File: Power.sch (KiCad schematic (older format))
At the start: 30 parts, among them J4 USB4125-GF-A, J5 S2B-PH-SM4-TB, U10 MCP73831T-2ATI_OT, U11 MIC2288YD5, U8 RT6150AGQW, U9 LP5907MFX-3.2

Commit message: Resolve DRC errors and add proper flagging
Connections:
- wire segments 83 -> 87
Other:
- moved on the sheet: C20, C23, J5, R21, R22, R25, U10

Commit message: layout wip
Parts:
- renumbered C17 to C18, C18 to C19, C19 to C20, C20 to C21, C21 to C22, C22 to C23, C23 to C24, C24 to C25, C25 to C26, J4 to J3, J5 to J4, R16 to R18, R17 to R19, R18 to R20, R19 to R21, R20 to R22, R21 to R23, R22 to R24, R23 to R25, R24 to R26, R25 to R27, R26 to R28, R27 to R29, U9 to U10, U10 to U11, U11 to U12, U8 to U9

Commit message: Add resistor details
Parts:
- R19, R20: Description (none) -> RES 5.1K OHM 1% 1/16W 0402; Manufacturer (none) -> Stackpole Electronics Inc; Part Number (none) -> RMCF0402FT5K10; Temp Range (none) -> -55°C +155°C
- R21: Description (none) -> RES 487K OHM 1% 1/16W 0402; Manufacturer (none) -> Stackpole Electronics Inc; Part Number (none) -> RMCF0402FT487K; Temp Range (none) -> -55°C +155°C
- R22: Description (none) -> RES 86.6K OHM 1% 1/16W 0402; Manufacturer (none) -> Stackpole Electronics Inc; Part Number (none) -> RMCF0402FT86K6; Temp Range (none) -> -55°C +155°C
- R23: Description (none) -> RES 300K OHM 1% 1/16W 0402; Manufacturer (none) -> Stackpole Electronics Inc; Part Number (none) -> RMCF0402FT300K; Temp Range (none) -> -55°C +155°C
- R24: Description (none) -> RES 180K OHM 1% 1/16W 0402; Manufacturer (none) -> Stackpole Electronics Inc; Part Number (none) -> RMCF0402FT180K; Temp Range (none) -> -55°C +155°C
- R25: Description (none) -> RES 0 OHM JUMPER 1/16W 0402; Manufacturer (none) -> Stackpole Electronics Inc; Part Number (none) -> RMCF0402ZT0R00; Temp Range (none) -> -55°C +155°C
- R27: Description (none) -> RES 10K OHM 1% 1/16W 0402; Manufacturer (none) -> Stackpole Electronics Inc; Part Number (none) -> RMCF0402FT10K0; Temp Range (none) -> -55°C +155°C
- R28: Description (none) -> RES 9.1K OHM 1% 1/16W 0402; Manufacturer (none) -> Stackpole Electronics Inc; Part Number (none) -> RMCF0402FT9K10; Temp Range (none) -> -55°C +155°C
- R29: Description (none) -> RES 3K OHM 1% 1/16W 0402; Manufacturer (none) -> Stackpole Electronics Inc; Part Number (none) -> RMCF0402FT3K00; Temp Range (none) -> -55°C +155°C
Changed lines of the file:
@@
 F 1 "86.6k" H 4720 4455 50  0000 L CNN
 F 2 "JetkovKiCADLib:R_0402_NoSilk" V 4580 4500 50  0001 C CNN
-F 3 "~" H 4650 4500 50  0001 C CNN
+F 3 "https://www.seielect.com/catalog/sei-rmcf_rmcp.pdf" H 4650 4500 50  0001 C CNN
+F 4 "RES 86.6K OHM 1% 1/16W 0402" H 4650 4500 50  0001 C CNN "Description"
+F 5 "Stackpole Electronics Inc" H 4650 4500 50  0001 C CNN "Manufacturer"
+F 6 "RMCF0402FT86K6" H 4650 4500 50  0001 C CNN "Part Number"
+F 7 "-55°C +155°C" H 4650 4500 50  0001 C CNN "Temp Range"
 	1    4650 4500
 	1    0    0    -1
@@
 F 1 "10k" H 6670 1905 50  0000 L CNN
 F 2 "JetkovKiCADLib:R_0402_NoSilk" V 6530 1950 50  0001 C CNN
-F 3 "~" H 6600 1950 50  0001 C CNN
+F 3 "https://www.seielect.com/catalog/sei-rmcf_rmcp.pdf" H 6600 1950 50  0001 C CNN
+F 4 "RES 10K OHM 1% 1/16W 0402" H 6600 1950 50  0001 C CNN "Description"
+F 5 "Stackpole Electronics Inc" H 6600 1950 50  0001 C CNN "Manufacturer"
+F 6 "RMCF0402FT10K0" H 6600 1950 50  0001 C CNN "Part Number"
+F 7 "-55°C +155°C" H 6600 1950 50  0001 C CNN "Temp Range"
 	1    6600 1950
 	1    0    0    -1
@@
 F 1 "487k" H 4720 4055 50  0000 L CNN
 F 2 "JetkovKiCADLib:R_0402_NoSilk" V 4580 4100 50  0001 C CNN
-F 3 "~" H 4650 4100 50  0001 C CNN
+F 3 "https://www.seielect.com/catalog/sei-rmcf_rmcp.pdf" H 4650 4100 50  0001 C CNN
+F 4 "RES 487K OHM 1% 1/16W 0402" H 4650 4100 50  0001 C CNN "Description"
+F 5 "Stackpole Electronics Inc" H 4650 4100 50  0001 C CNN "Manufacturer"
+F 6 "RMCF0402FT487K" H 4650 4100 50  0001 C CNN "Part Number"
+F 7 "-55°C +155°C" H 4650 4100 50  0001 C CNN "Temp Range"
 	1    4650 4100
 	1    0    0    -1
@@
 F 1 "9.1k" H 7720 3655 50  0000 L CNN
 F 2 "JetkovKiCADLib:R_0402_NoSilk" V 7580 3700 50  0001 C CNN
-F 3 "~" H 7650 3700 50  0001 C CNN
+F 3 "https://www.seielect.com/catalog/sei-rmcf_rmcp.pdf" H 7650 3700 50  0001 C CNN
+F 4 "RES 9.1K OHM 1% 1/16W 0402" H 7650 3700 50  0001 C CNN "Description"
+F 5 "Stackpole Electronics Inc" H 7650 3700 50  0001 C CNN "Manufacturer"
+F 6 "RMCF0402FT9K10" H 7650 3700 50  0001 C CNN "Part Number"
+F 7 "-55°C +155°C" H 7650 3700 50  0001 C CNN "Temp Range"
 	1    7650 3700
 	1    0    0    -1
@@
 F 1 "3k" H 7720 4055 50  0000 L CNN
 F 2 "JetkovKiCADLib:R_0402_NoSilk" V 7580 4100 50  0001 C CNN
-F 3 "~" H 7650 4100 50  0001 C CNN
+F 3 "https://www.seielect.com/catalog/sei-rmcf_rmcp.pdf" H 7650 4100 50  0001 C CNN
+F 4 "RES 3K OHM 1% 1/16W 0402" H 7650 4100 50  0001 C CNN "Description"
+F 5 "Stackpole Electronics Inc" H 7650 4100 50  0001 C CNN "Manufacturer"
+F 6 "RMCF0402FT3K00" H 7650 4100 50  0001 C CNN "Part Number"
+F 7 "-55°C +155°C" H 7650 4100 50  0001 C CNN "Temp Range"
 	1    7650 4100
 	1    0    0    -1
@@
 F 1 "5.1k" H 4070 1955 50  0000 L CNN
 F 2 "JetkovKiCADLib:R_0402_NoSilk" V 3930 2000 50  0001 C CNN
-F 3 "~" H 4000 2000 50  0001 C CNN
+F 3 "https://www.seielect.com/catalog/sei-rmcf_rmcp.pdf" H 4000 2000 50  0001 C CNN
+F 4 "RES 5.1K OHM 1% 1/16W 0402" H 4000 2000 50  0001 C CNN "Description"
+F 5 "Stackpole Electronics Inc" H 4000 2000 50  0001 C CNN "Manufacturer"
+F 6 "RMCF0402FT5K10" H 4000 2000 50  0001 C CNN "Part Number"
+F 7 "-55°C +155°C" H 4000 2000 50  0001 C CNN "Temp Range"
 	1    4000 2000
 	-1   0    0    -1
@@
 F 1 "5.1k" H 4270 1955 50  0000 L CNN
 F 2 "JetkovKiCADLib:R_0402_NoSilk" V 4130 2000 50  0001 C CNN
-F 3 "~" H 4200 2000 50  0001 C CNN
+F 3 "https://www.seielect.com/catalog/sei-rmcf_rmcp.pdf" H 4200 2000 50  0001 C CNN
+F 4 "RES 5.1K OHM 1% 1/16W 0402" H 4200 2000 50  0001 C CNN "Description"
+F 5 "Stackpole Electronics Inc" H 4200 2000 50  0001 C CNN "Manufacturer"
+F 6 "RMCF0402FT5K10" H 4200 2000 50  0001 C CNN "Part Number"
+F 7 "-55°C +155°C" H 4200 2000 50  0001 C CNN "Temp Range"
 	1    4200 2000
 	1    0    0    -1
@@
 F 1 "0R" V 5450 5150 50  0000 L CNN
 F 2 "JetkovKiCADLib:R_0402_NoSilk" V 5480 5300 50  0001 C CNN
-F 3 "~" H 5550 5300 50  0001 C CNN
+F 3 "https://www.seielect.com/catalog/sei-rmcf_rmcp.pdf" H 5550 5300 50  0001 C CNN
+F 4 "RES 0 OHM JUMPER 1/16W 0402" H 5550 5300 50  0001 C CNN "Description"
+F 5 "Stackpole Electronics Inc" H 5550 5300 50  0001 C CNN "Manufacturer"
+F 6 "RMCF0402ZT0R00" H 5550 5300 50  0001 C CNN "Part Number"
+F 7 "-55°C +155°C" H 5550 5300 50  0001 C CNN "Temp Range"
 	1    5550 5300
 	0    1    1    0
@@
 F 1 "180k" V 5550 2000 50  0000 L CNN
 F 2 "JetkovKiCADLib:R_0402_NoSilk" V 5380 2100 50  0001 C CNN
-F 3 "~" H 5450 2100 50  0001 C CNN
+F 3 "https://www.seielect.com/catalog/sei-rmcf_rmcp.pdf" H 5450 2100 50  0001 C CNN
+F 4 "RES 180K OHM 1% 1/16W 0402" H 5450 2100 50  0001 C CNN "Description"
+F 5 "Stackpole Electronics Inc" H 5450 2100 50  0001 C CNN "Manufacturer"
+F 6 "RMCF0402FT180K" H 5450 2100 50  0001 C CNN "Part Number"
+F 7 "-55°C +155°C" H 5450 2100 50  0001 C CNN "Temp Range"
 	1    5450 2100
 	0    -1   -1   0
@@
 F 1 "300k" H 5320 2255 50  0000 L CNN
 F 2 "JetkovKiCADLib:R_0402_NoSilk" V 5180 2300 50  0001 C CNN
-F 3 "~" H 5250 2300 50  0001 C CNN
+F 3 "https://www.seielect.com/catalog/sei-rmcf_rmcp.pdf" H 5250 2300 50  0001 C CNN
+F 4 "RES 300K OHM 1% 1/16W 0402" H 5250 2300 50  0001 C CNN "Description"
+F 5 "Stackpole Electronics Inc" H 5250 2300 50  0001 C CNN "Manufacturer"
+F 6 "RMCF0402FT300K" H 5250 2300 50  0001 C CNN "Part Number"
+F 7 "-55°C +155°C" H 5250 2300 50  0001 C CNN "Temp Range"
 	1    5250 2300
 	1    0    0    -1

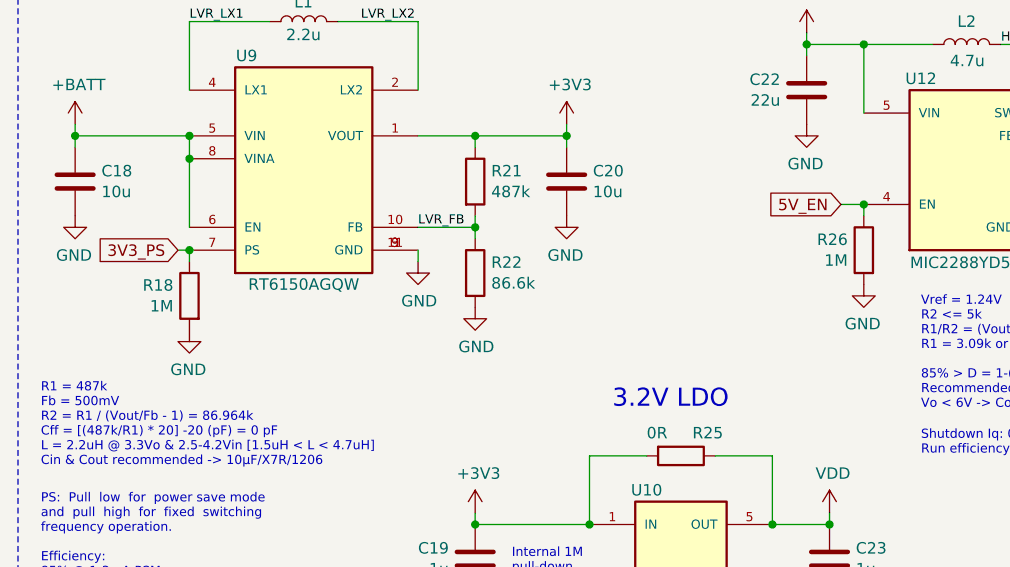
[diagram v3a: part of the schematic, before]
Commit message: Fill in component info, reduce uniqe resistors. cleanup
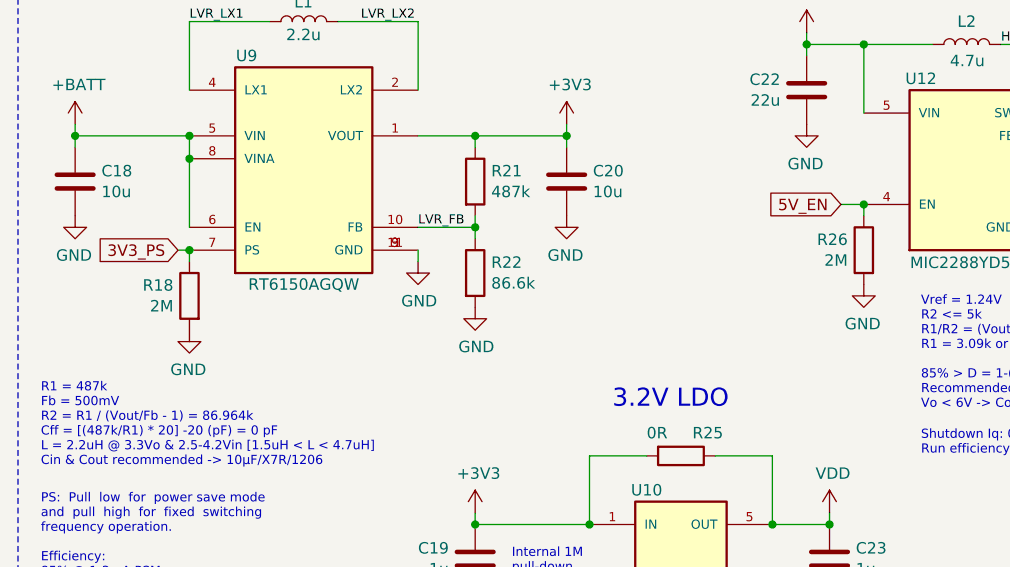
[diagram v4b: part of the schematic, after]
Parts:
- R18, R26: value 1M -> 2M; Description (none) -> RES 2M OHM 1% 1/16W 0402; Manufacturer (none) -> Stackpole Electronics Inc; Part Number (none) -> RMCF0402FT2M00; Temp Range (none) -> -55°C +155°C
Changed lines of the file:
@@
 P 6350 4400
 F 0 "R26" H 6420 4446 50  0000 L CNN
-F 1 "1M" H 6420 4355 50  0000 L CNN
+F 1 "2M" H 6420 4355 50  0000 L CNN
 F 2 "JetkovKiCADLib:R_0402_NoSilk" V 6280 4400 50  0001 C CNN
-F 3 "~" H 6350 4400 50  0001 C CNN
+F 3 "https://www.seielect.com/catalog/sei-rmcf_rmcp.pdf" H 6350 4400 50  0001 C CNN
+F 4 "RES 2M OHM 1% 1/16W 0402" H 6350 4400 50  0001 C CNN "Description"
+F 5 "Stackpole Electronics Inc" H 6350 4400 50  0001 C CNN "Manufacturer"
+F 6 "RMCF0402FT2M00" H 6350 4400 50  0001 C CNN "Part Number"
+F 7 "-55°C +155°C" H 6350 4400 50  0001 C CNN "Temp Range"
 	1    6350 4400
 	-1   0    0    -1
@@
 P 3400 4600
 F 0 "R18" H 3470 4646 50  0000 L CNN
-F 1 "1M" H 3470 4555 50  0000 L CNN
+F 1 "2M" H 3470 4555 50  0000 L CNN
 F 2 "JetkovKiCADLib:R_0402_NoSilk" V 3330 4600 50  0001 C CNN
-F 3 "~" H 3400 4600 50  0001 C CNN
+F 3 "https://www.seielect.com/catalog/sei-rmcf_rmcp.pdf" H 3400 4600 50  0001 C CNN
+F 4 "RES 2M OHM 1% 1/16W 0402" H 3400 4600 50  0001 C CNN "Description"
+F 5 "Stackpole Electronics Inc" H 3400 4600 50  0001 C CNN "Manufacturer"
+F 6 "RMCF0402FT2M00" H 3400 4600 50  0001 C CNN "Part Number"
+F 7 "-55°C +155°C" H 3400 4600 50  0001 C CNN "Temp Range"
 	1    3400 4600
 	-1   0    0    -1

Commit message: Add TVS diodes, resistor for piezo drive, and test point
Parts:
- added D7: D_Schottky_ALT, JetkovKiCADLib:NSPU3051, symbol Device:D_Schottky_ALT
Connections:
- wire segments 87 -> 90
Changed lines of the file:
@@
 L power:PWR_FLAG #FLG01
 U 1 1 6075A4E8
-P 3750 1500
-F 0 "#FLG01" H 3750 1575 50  0001 C CNN
-F 1 "PWR_FLAG" V 3738 1802 50  0000 C CNN
-F 2 "" H 3750 1500 50  0001 C CNN
-F 3 "~" H 3750 1500 50  0001 C CNN
-	1    3750 1500
-	0    1    1    0
+P 3900 1500
+F 0 "#FLG01" H 3900 1575 50  0001 C CNN
+F 1 "PWR_FLAG" H 3858 1428 50  0000 C CNN
+F 2 "" H 3900 1500 50  0001 C CNN
+F 3 "~" H 3900 1500 50  0001 C CNN
+	1    3900 1500
+	1    0    0    -1
 $EndComp
-Wire Wire Line
-	3750 1500 3700 1500
 Connection ~ 3700 1500
 $Comp
@@
 Wire Wire Line
 	7900 2000 7950 2000
+$Comp
+L Device:D_Schottky_ALT D?
+U 1 1 6047AD75
+P 4150 1500
+AR Path="/6047AD75" Ref="D?"  Part="1"
+AR Path="/60656A7D/6047AD75" Ref="D7"  Part="1"
+F 0 "D7" H 4150 1400 50  0000 C CNN
+F 1 "D_Schottky_ALT" H 4150 1626 50  0001 C CNN
+F 2 "JetkovKiCADLib:NSPU3051" H 4150 1500 50  0001 C CNN
+F 3 "http://www.onsemi.com/pub/Collateral/NSPU3051-D.PDF" H 4150 1500 50  0001 C CNN
+F 4 "TVS DIODE 5.5V 9.5V 2X2DFN" H 4150 1500 50  0001 C CNN "Description"
+F 5 "ON Semiconductor" H 4150 1500 50  0001 C CNN "Manufacturer"
+F 6 "NSPU3051N2T5G" H 4150 1500 50  0001 C CNN "Part Number"
+F 7 "-65°C +150°C" H 4150 1500 50  0001 C CNN "Temp Range"
+	1    4150 1500
+	1    0    0    1
+$EndComp
+$Comp
+L power:GND #PWR085
+U 1 1 6047D1DE
+P 4400 1600
+F 0 "#PWR085" H 4400 1350 50  0001 C CNN
+F 1 "GND" H 4405 1427 50  0000 C CNN
+F 2 "" H 4400 1600 50  0001 C CNN
+F 3 "" H 4400 1600 50  0001 C CNN
+	1    4400 1600
+	-1   0    0    -1
+$EndComp
+Wire Wire Line
+	4300 1500 4400 1500
+Wire Wire Line
+	4400 1500 4400 1600
+Wire Wire Line
+	3700 1500 3900 1500
+Connection ~ 3900 1500
+Wire Wire Line
+	3900 1500 4000 1500
 $EndSCHEMATC
